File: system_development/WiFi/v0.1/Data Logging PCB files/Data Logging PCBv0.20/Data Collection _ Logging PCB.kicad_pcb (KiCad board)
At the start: 2 copper layers, 34.3 x 53.3 mm, 7 parts, among them U1 TC2014-3.3VxCTTR

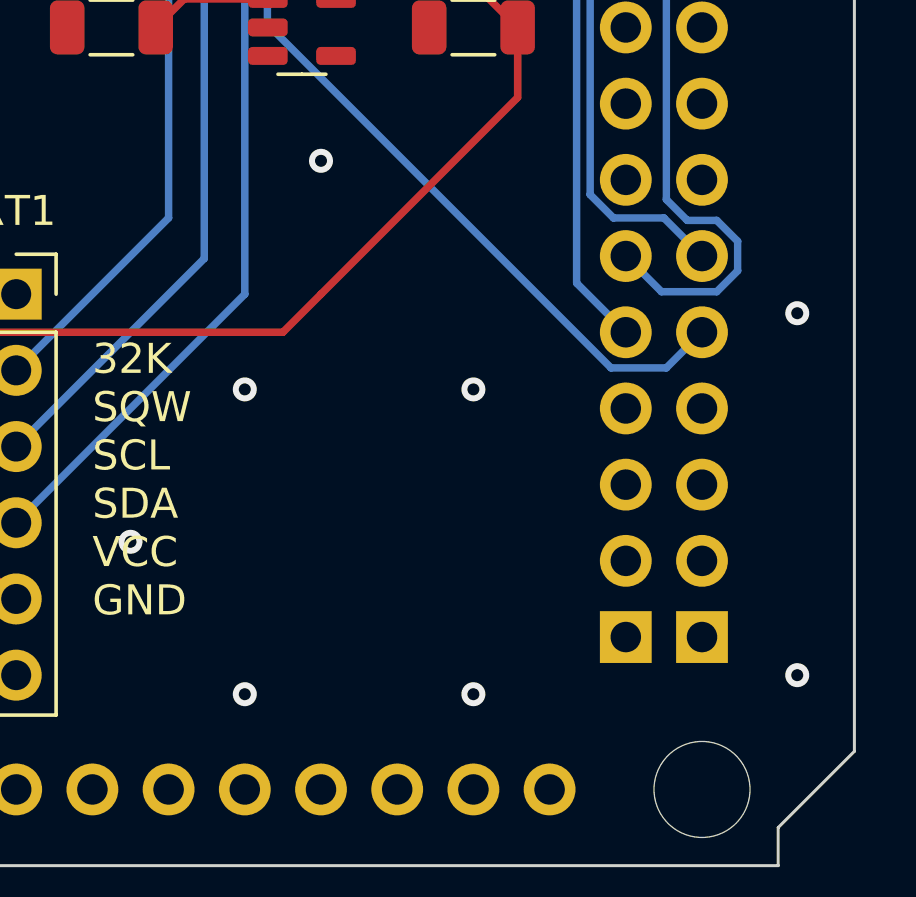
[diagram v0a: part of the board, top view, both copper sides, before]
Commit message: Updated Wifi Code
Updated Wifi code to reflect some of the changes made to the cellular code, order of operations, failsafes.
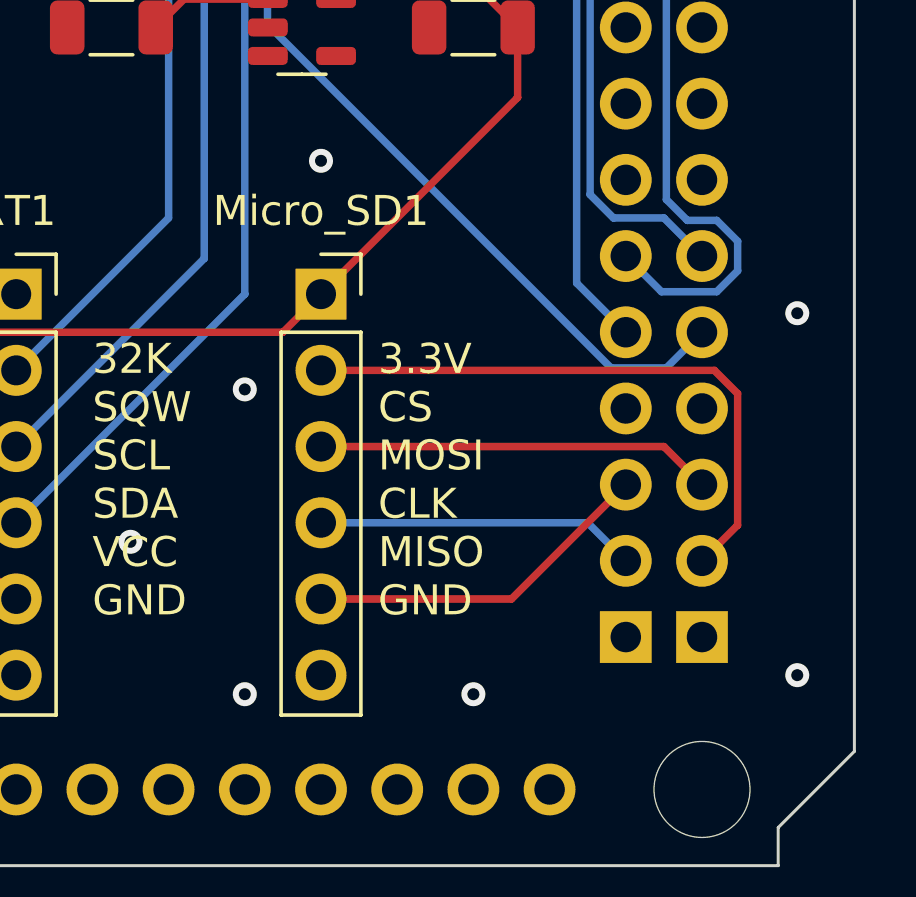
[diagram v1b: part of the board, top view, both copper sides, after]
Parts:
- added Micro_SD1: microSD_small, Connector_PinSocket_2.54mm:PinSocket_1x06_P2.54mm_Vertical, F.Cu at (188.0, 108.0)
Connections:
- XA1 pad D50: unconnected-(XA1-PadD50) -> Net-(Micro_SD1-MISO)
- XA1 pad D51: unconnected-(XA1-PadD51) -> Net-(Micro_SD1-MOSI)
- XA1 pad D52: unconnected-(XA1-PadD52) -> Net-(Micro_SD1-CLK)
- XA1 pad D53: unconnected-(XA1-D53_SS-PadD53) -> Net-(Micro_SD1-CS)
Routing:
- net Net-(Micro_SD1-CS): track 0.00 -> 20.3 mm
- net Net-(Micro_SD1-MOSI): track 0.00 -> 13.2 mm
- net Net-(Micro_SD1-MISO): track 0.00 -> 11.7 mm
- net Net-(Micro_SD1-CLK): track 0.00 -> 10.7 mm
- net GND: vias 11 -> 10
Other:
- board text added: "3.3V CS MOSI CLK MISO GND"
- board text added: "Datalogging v0.2 5/16/2024 Nicholas Liger ARTS Lab - USC"
- board text removed: "Wifi-Datalogging v0.1 6/21/2024 Nicholas Liger ARTS Lab - USC"
